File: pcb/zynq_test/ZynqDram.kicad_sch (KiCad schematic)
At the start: 44 parts, among them U202 XC7Z020-2CLG400I, U401 MT41K256M16TW-107, U402 MT41K256M16TW-107

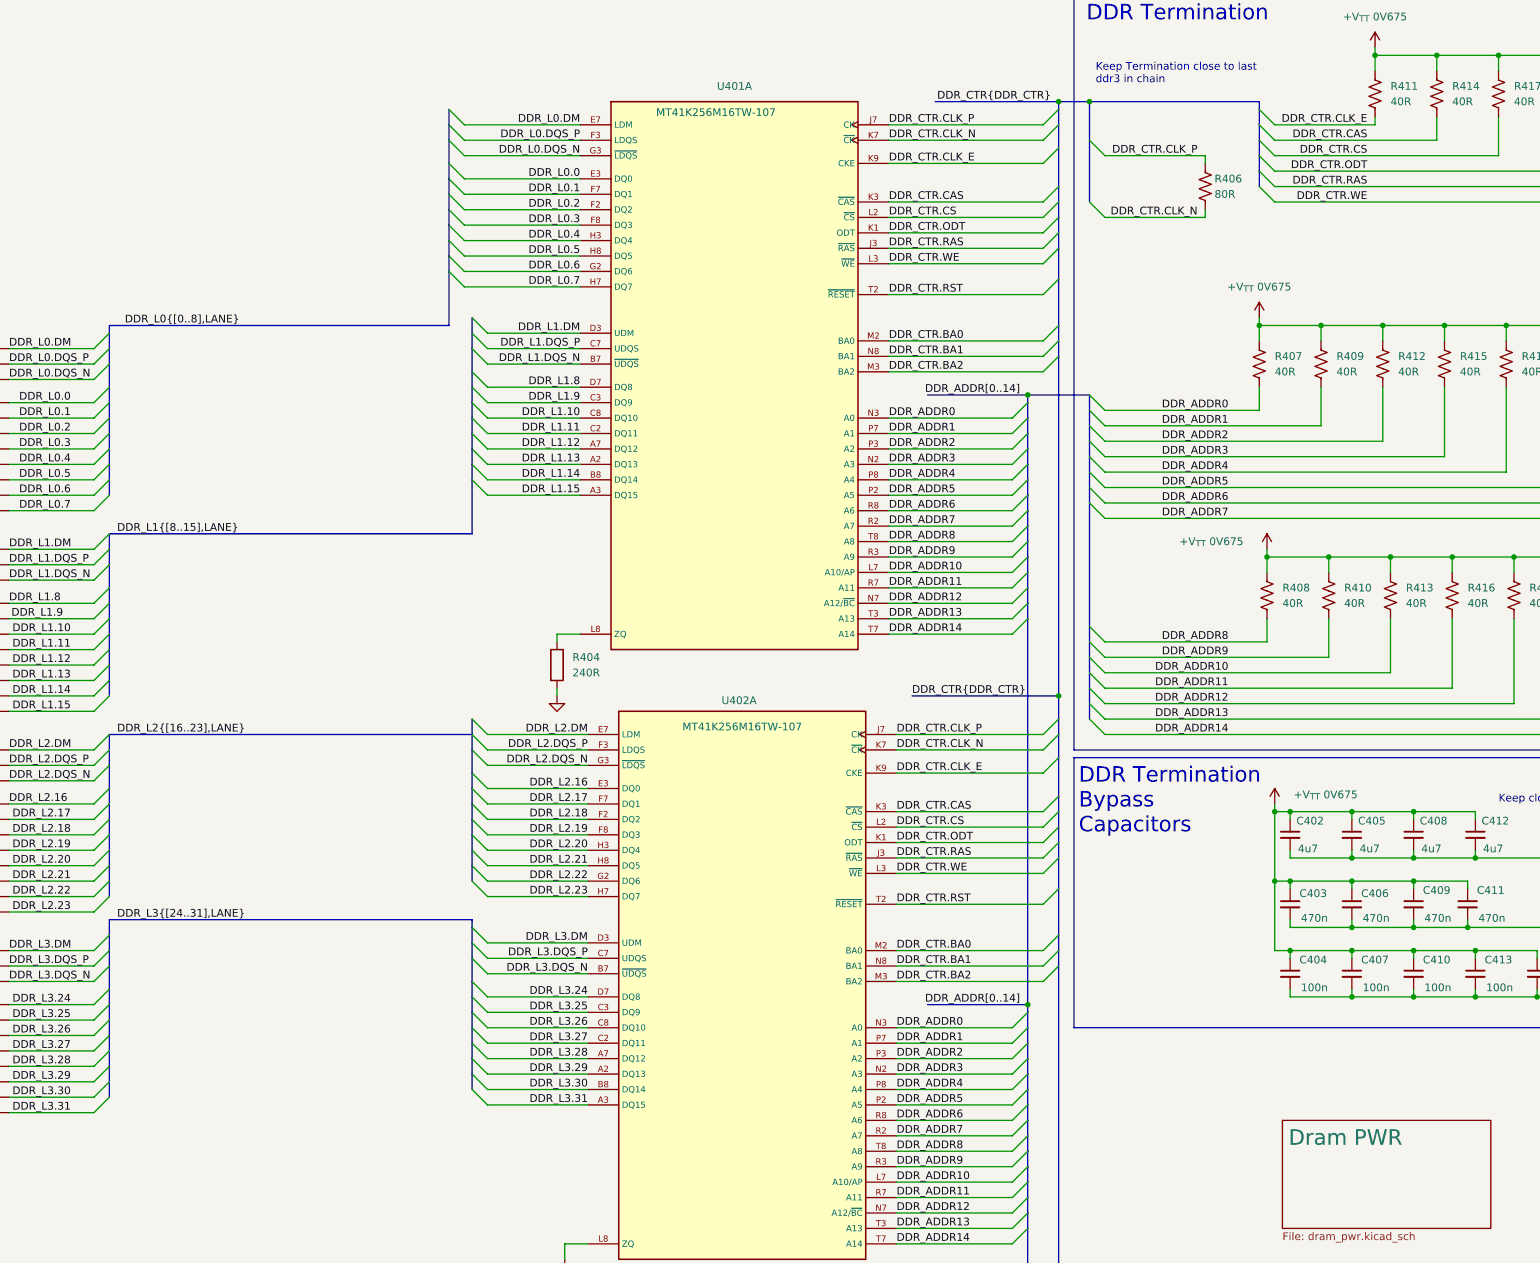
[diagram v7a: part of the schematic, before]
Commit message: Finished to first ddr ic
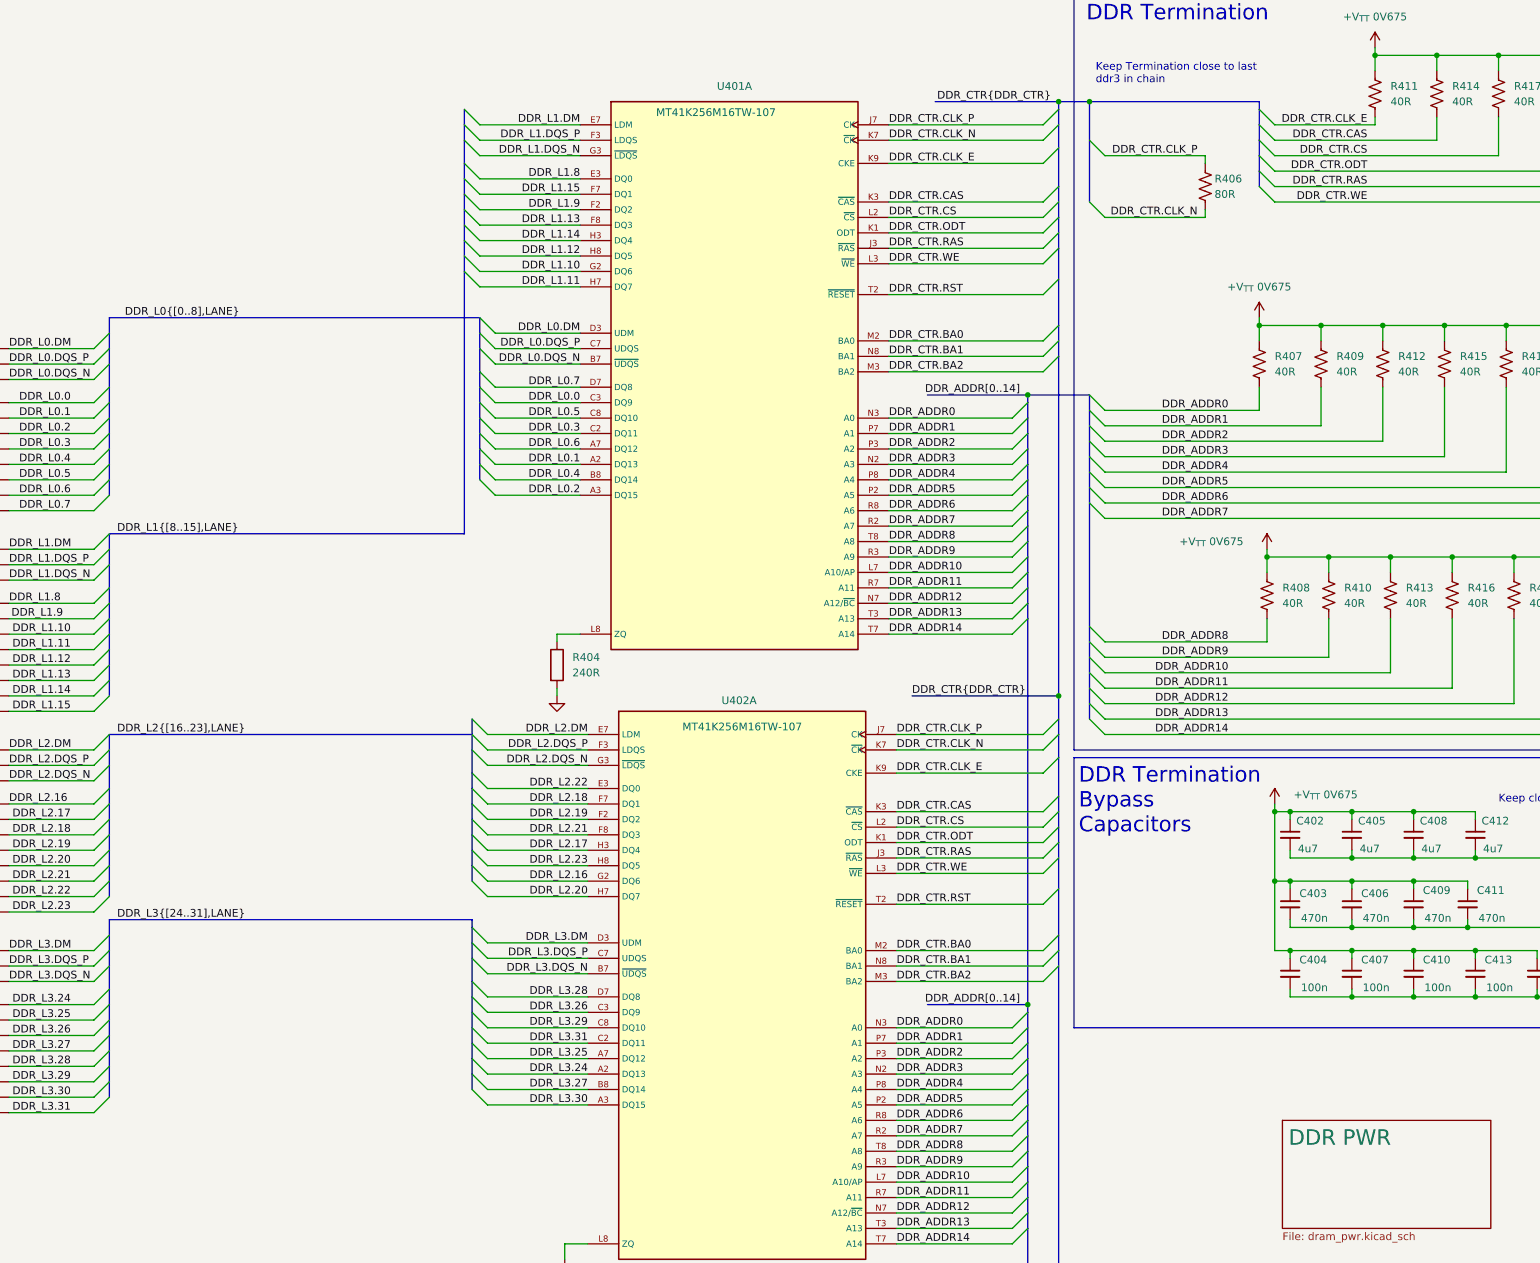
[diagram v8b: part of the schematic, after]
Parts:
- U202: footprint Package_BGA:Xilinx_CLG400 -> Zynq:Zynq_Z7020-2CLG400I_W_Delay
- U401, U402: footprint dram:BGA96C80P9X16_1400X800X120 -> dram:BGA96C80P9X16_1400X800X120_pinDelays
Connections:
- net DDR_L0.0: now also U401.C3 (DQ9); no longer U401.E3 (DQ0)
- net DDR_L0.1: now also U401.A2 (DQ13); no longer U401.F7 (DQ1)
- net DDR_L0.2: now also U401.A3 (DQ15); no longer U401.F2 (DQ2)
- net DDR_L0.3: now also U401.C2 (DQ11); no longer U401.F8 (DQ3)
- net DDR_L0.4: now also U401.B8 (DQ14); no longer U401.H3 (DQ4)
- net DDR_L0.5: now also U401.C8 (DQ10); no longer U401.H8 (DQ5)
- net DDR_L0.6: now also U401.A7 (DQ12); no longer U401.G2 (DQ6)
- net DDR_L0.7: now also U401.D7 (DQ8); no longer U401.H7 (DQ7)
- net DDR_L0.DM: now also U401.D3 (UDM); no longer U401.E7 (LDM)
- net DDR_L0.DQS_N: now also U401.B7 (~{UDQS}); no longer U401.G3 (~{LDQS})
- net DDR_L0.DQS_P: now also U401.C7 (UDQS); no longer U401.F3 (LDQS)
- net DDR_L1.10: now also U401.G2 (DQ6); no longer U401.C8 (DQ10)
- net DDR_L1.11: now also U401.H7 (DQ7); no longer U401.C2 (DQ11)
- net DDR_L1.12: now also U401.H8 (DQ5); no longer U401.A7 (DQ12)
- net DDR_L1.13: now also U401.F8 (DQ3); no longer U401.A2 (DQ13)
- net DDR_L1.14: now also U401.H3 (DQ4); no longer U401.B8 (DQ14)
- net DDR_L1.15: now also U401.F7 (DQ1); no longer U401.A3 (DQ15)
- net DDR_L1.8: now also U401.E3 (DQ0); no longer U401.D7 (DQ8)
- net DDR_L1.9: now also U401.F2 (DQ2); no longer U401.C3 (DQ9)
- net DDR_L1.DM: now also U401.E7 (LDM); no longer U401.D3 (UDM)
- net DDR_L1.DQS_N: now also U401.G3 (~{LDQS}); no longer U401.B7 (~{UDQS})
- net DDR_L1.DQS_P: now also U401.F3 (LDQS); no longer U401.C7 (UDQS)
- net DDR_L2.16: now also U402.G2 (DQ6); no longer U402.E3 (DQ0)
- net DDR_L2.17: now also U402.H3 (DQ4); no longer U402.F7 (DQ1)
- net DDR_L2.18: now also U402.F7 (DQ1); no longer U402.F2 (DQ2)
- net DDR_L2.19: now also U402.F2 (DQ2); no longer U402.F8 (DQ3)
- net DDR_L2.20: now also U402.H7 (DQ7); no longer U402.H3 (DQ4)
- net DDR_L2.21: now also U402.F8 (DQ3); no longer U402.H8 (DQ5)
- net DDR_L2.22: now also U402.E3 (DQ0); no longer U402.G2 (DQ6)
- net DDR_L2.23: now also U402.H8 (DQ5); no longer U402.H7 (DQ7)
- net DDR_L3.24: now also U402.A2 (DQ13); no longer U402.D7 (DQ8)
- net DDR_L3.25: now also U402.A7 (DQ12); no longer U402.C3 (DQ9)
- net DDR_L3.26: now also U402.C3 (DQ9); no longer U402.C8 (DQ10)
- net DDR_L3.27: now also U402.B8 (DQ14); no longer U402.C2 (DQ11)
- net DDR_L3.28: now also U402.D7 (DQ8); no longer U402.A7 (DQ12)
- net DDR_L3.29: now also U402.C8 (DQ10); no longer U402.A2 (DQ13)
- net DDR_L3.30: now also U402.A3 (DQ15); no longer U402.B8 (DQ14)
- net DDR_L3.31: now also U402.C2 (DQ11); no longer U402.A3 (DQ15)
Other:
- sheet Dram PWR renamed DDR PWR
